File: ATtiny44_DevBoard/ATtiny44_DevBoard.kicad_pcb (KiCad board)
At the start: 2 copper layers, 48.3 x 42.5 mm, 19 parts, among them J1 Conn_01x08, J2 Conn_02x03_Odd_Even, J3 Conn_01x08, U1 ATtiny44A-SSU, Y1 Crystal 12MHz

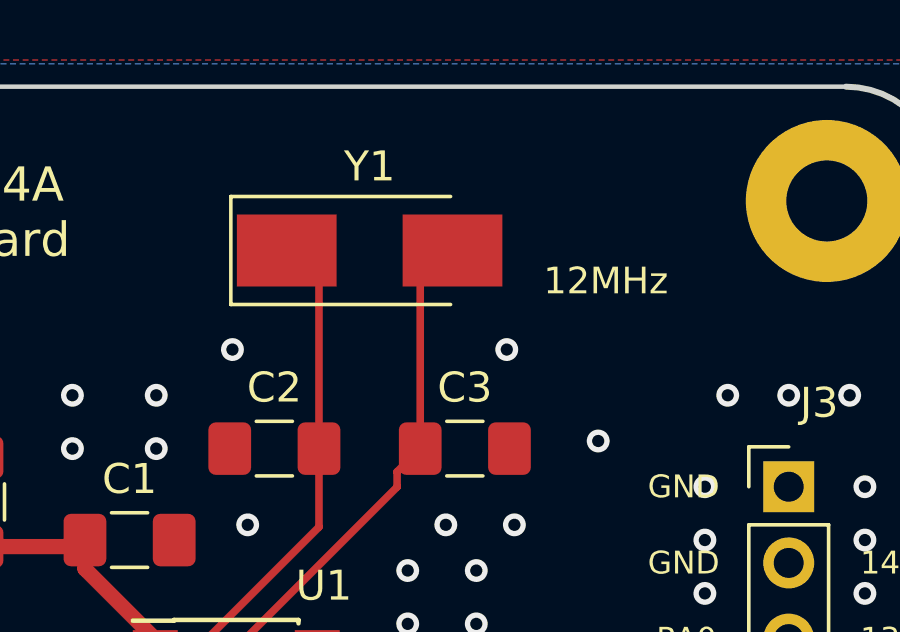
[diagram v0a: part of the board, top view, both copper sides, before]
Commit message: Replace SMD quartz with simpler THT one
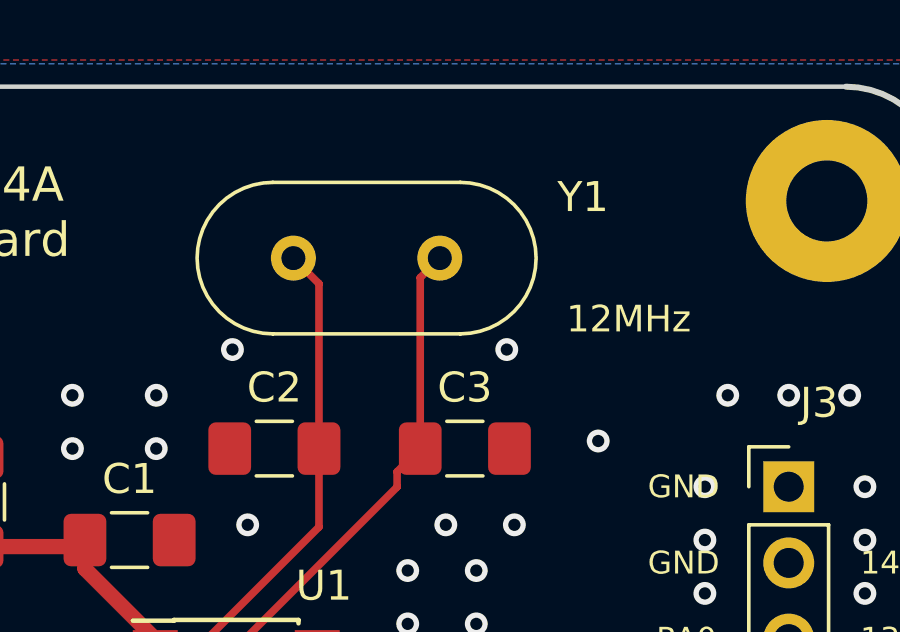
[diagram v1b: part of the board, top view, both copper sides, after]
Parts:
- Y1: footprint Crystal:Crystal_SMD_Abracon_ABM3-2Pin_5.0x3.2mm_HandSoldering -> Crystal:Crystal_HC49-U_Vertical
- moved Y1 2.55 mm to (150.9, 75.7)
- moved REF** 0.51 mm to (156.5, 80.3)
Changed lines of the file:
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@@
       (drillshape 0)
       (scaleselection 1)
-      (outputdirectory "gerber/"))
+      (outputdirectory "gerbers/"))
   )
   (net 0 "")
@@
     )
   )
-  (module Crystal:Crystal_SMD_Abracon_ABM3-2Pin_5.0x3.2mm_HandSoldering (layer F.Cu)
-    (at 153.416 75.438)
-    (descr "Abracon Miniature Ceramic Smd Crystal ABM3 http://www.abracon.com/Resonators/abm3.pdf, hand-soldering, 5.0x3.2mm^2 package")
-    (tags "SMD SMT crystal hand-soldering")
-    (attr smd)
-    (fp_text reference Y1 (at 0 -2.8) (layer F.SilkS)
-      (effects (font (size 1 1) (thickness 0.15)))
-    )
-    (fp_text value "Crystal 12MHz" (at 0 2.8) (layer F.Fab)
-      (effects (font (size 1 1) (thickness 0.15)))
-    )
-    (fp_text user %R (at 0 0) (layer F.Fab)
-      (effects (font (size 1 1) (thickness 0.15)))
-    )
-    (fp_line (start -2.3 -1.6) (end 2.3 -1.6) (layer F.Fab) (width 0.1))
-    (fp_line (start 2.3 -1.6) (end 2.5 -1.4) (layer F.Fab) (width 0.1))
-    (fp_line (start 2.5 -1.4) (end 2.5 1.4) (layer F.Fab) (width 0.1))
-    (fp_line (start 2.5 1.4) (end 2.3 1.6) (layer F.Fab) (width 0.1))
-    (fp_line (start 2.3 1.6) (end -2.3 1.6) (layer F.Fab) (width 0.1))
-    (fp_line (start -2.3 1.6) (end -2.5 1.4) (layer F.Fab) (width 0.1))
-    (fp_line (start -2.5 1.4) (end -2.5 -1.4) (layer F.Fab) (width 0.1))
-    (fp_line (start -2.5 -1.4) (end -2.3 -1.6) (layer F.Fab) (width 0.1))
-    (fp_line (start -2.5 0.6) (end -1.5 1.6) (layer F.Fab) (width 0.1))
-    (fp_line (start 2.7 -1.8) (end -4.625 -1.8) (layer F.SilkS) (width 0.12))
-    (fp_line (start -4.625 -1.8) (end -4.625 1.8) (layer F.SilkS) (width 0.12))
-    (fp_line (start -4.625 1.8) (end 2.7 1.8) (layer F.SilkS) (width 0.12))
-    (fp_line (start -4.7 -1.9) (end -4.7 1.9) (layer F.CrtYd) (width 0.05))
-    (fp_line (start -4.7 1.9) (end 4.7 1.9) (layer F.CrtYd) (width 0.05))
-    (fp_line (start 4.7 1.9) (end 4.7 -1.9) (layer F.CrtYd) (width 0.05))
-    (fp_line (start 4.7 -1.9) (end -4.7 -1.9) (layer F.CrtYd) (width 0.05))
-    (fp_circle (center 0 0) (end 0.5 0) (layer F.Adhes) (width 0.1))
-    (fp_circle (center 0 0) (end 0.416667 0) (layer F.Adhes) (width 0.166667))
-    (fp_circle (center 0 0) (end 0.266667 0) (layer F.Adhes) (width 0.166667))
-    (fp_circle (center 0 0) (end 0.116667 0) (layer F.Adhes) (width 0.233333))
-    (pad 1 smd rect (at -2.7625 0) (size 3.325 2.4) (layers F.Cu F.Paste F.Mask)
-      (net 3 /XTAL1))
-    (pad 2 smd rect (at 2.7625 0) (size 3.325 2.4) (layers F.Cu F.Paste F.Mask)
-      (net 4 /XTAL2))
-    (model ${KISYS3DMOD}/Crystal.3dshapes/Crystal_SMD_Abracon_ABM3-2Pin_5.0x3.2mm_HandSoldering.wrl
-      (at (xyz 0 0 0))
-      (scale (xyz 1 1 1))
-      (rotate (xyz 0 0 0))
-    )
-  )
   (module MountingHole:MountingHole_2.7mm_M2.5_Pad (layer F.Cu)
     (at 128.016 73.787)
@@
   )
   (module Symbol:KiCad-Logo2_6mm_SilkScreen (layer B.Cu)
-    (at 156.464 79.756 180)
+    (at 156.464 80.264 180)
     (descr "KiCad Logo")
     (tags "Logo KiCad")
@@
       (xy -2.549664 -1.91989) (xy -2.469928 -1.911165) (xy -2.400256 -1.919918)) (layer B.SilkS) (width 0.01))
   )
+  (module Crystal:Crystal_HC49-U_Vertical (layer F.Cu)
+    (at 150.876 75.692)
+    (descr "Crystal THT HC-49/U http://5hertz.com/pdfs/04404_D.pdf")
+    (tags "THT crystalHC-49/U")
+    (fp_text reference Y1 (at 9.652 -2.032) (layer F.SilkS)
+      (effects (font (size 1 1) (thickness 0.15)))
+    )
+    (fp_text value "Crystal 12MHz" (at 2.44 3.525) (layer F.Fab)
+      (effects (font (size 1 1) (thickness 0.15)))
+    )
+    (fp_text user %R (at 2.44 0) (layer F.Fab)
+      (effects (font (size 1 1) (thickness 0.15)))
+    )
+    (fp_line (start -0.685 -2.325) (end 5.565 -2.325) (layer F.Fab) (width 0.1))
+    (fp_line (start -0.685 2.325) (end 5.565 2.325) (layer F.Fab) (width 0.1))
+    (fp_line (start -0.56 -2) (end 5.44 -2) (layer F.Fab) (width 0.1))
+    (fp_line (start -0.56 2) (end 5.44 2) (layer F.Fab) (width 0.1))
+    (fp_line (start -0.685 -2.525) (end 5.565 -2.525) (layer F.SilkS) (width 0.12))
+    (fp_line (start -0.685 2.525) (end 5.565 2.525) (layer F.SilkS) (width 0.12))
+    (fp_line (start -3.5 -2.8) (end -3.5 2.8) (layer F.CrtYd) (width 0.05))
+    (fp_line (start -3.5 2.8) (end 8.4 2.8) (layer F.CrtYd) (width 0.05))
+    (fp_line (start 8.4 2.8) (end 8.4 -2.8) (layer F.CrtYd) (width 0.05))
+    (fp_line (start 8.4 -2.8) (end -3.5 -2.8) (layer F.CrtYd) (width 0.05))
+    (fp_arc (start -0.685 0) (end -0.685 -2.325) (angle -180) (layer F.Fab) (width 0.1))
+    (fp_arc (start 5.565 0) (end 5.565 -2.325) (angle 180) (layer F.Fab) (width 0.1))
+    (fp_arc (start -0.56 0) (end -0.56 -2) (angle -180) (layer F.Fab) (width 0.1))
+    (fp_arc (start 5.44 0) (end 5.44 -2) (angle 180) (layer F.Fab) (width 0.1))
+    (fp_arc (start -0.685 0) (end -0.685 -2.525) (angle -180) (layer F.SilkS) (width 0.12))
+    (fp_arc (start 5.565 0) (end 5.565 -2.525) (angle 180) (layer F.SilkS) (width 0.12))
+    (pad 1 thru_hole circle (at 0 0) (size 1.5 1.5) (drill 0.8) (layers *.Cu *.Mask)
+      (net 3 /XTAL1))
+    (pad 2 thru_hole circle (at 4.88 0) (size 1.5 1.5) (drill 0.8) (layers *.Cu *.Mask)
+      (net 4 /XTAL2))
+    (model ${KISYS3DMOD}/Crystal.3dshapes/Crystal_HC49-U_Vertical.wrl
+      (at (xyz 0 0 0))
+      (scale (xyz 1 1 1))
+      (rotate (xyz 0 0 0))
+    )
+  )
   (gr_text "Rev 1.0" (at 135.128 109.728) (layer F.SilkS)
     (effects (font (size 1.143 1.143) (thickness 0.1778)))
@@
     (effects (font (size 0.762 0.762) (thickness 0.127)))
   )
-  (gr_text 12MHz (at 161.29 76.454) (layer F.SilkS)
+  (gr_text 12MHz (at 162.052 77.724) (layer F.SilkS)
     (effects (font (size 0.889 0.889) (thickness 0.1524)))
   )
@@
   (segment (start 130.556 89.662) (end 129.286 88.392) (width 0.254) (layer F.Cu) (net 3) (status 20))
   (segment (start 146.271 89.662) (end 130.556 89.662) (width 0.254) (layer F.Cu) (net 3) (status 10))
-  (segment (start 151.7285 76.513) (end 150.6535 75.438) (width 0.254) (layer F.Cu) (net 3))
-  (segment (start 151.7285 82.042) (end 151.7285 76.513) (width 0.254) (layer F.Cu) (net 3))
+  (segment (start 151.7285 76.5445) (end 150.876 75.692) (width 0.254) (layer F.Cu) (net 3))
+  (segment (start 151.7285 82.042) (end 151.7285 76.5445) (width 0.254) (layer F.Cu) (net 3))
   (segment (start 146.721 90.932) (end 146.271 90.932) (width 0.254) (layer F.Cu) (net 4) (status 30))
   (segment (start 154.332153 83.320847) (end 146.721 90.932) (width 0.254) (layer F.Cu) (net 4) (status 20))
@@
   (segment (start 155.1035 82.042) (end 154.332153 82.813347) (width 0.254) (layer F.Cu) (net 4) (status 10))
   (segment (start 146.271 90.932) (end 129.286 90.932) (width 0.254) (layer F.Cu) (net 4) (status 30))
-  (segment (start 155.1035 76.513) (end 156.1785 75.438) (width 0.254) (layer F.Cu) (net 4))
-  (segment (start 155.1035 82.042) (end 155.1035 76.513) (width 0.254) (layer F.Cu) (net 4))
+  (segment (start 155.1035 76.3445) (end 155.756 75.692) (width 0.254) (layer F.Cu) (net 4))
+  (segment (start 155.1035 82.042) (end 155.1035 76.3445) (width 0.254) (layer F.Cu) (net 4))
   (segment (start 159.004 107.6595) (end 158.496 107.1515) (width 0.254) (layer F.Cu) (net 5) (status 30))
   (segment (start 163.322 107.6595) (end 159.004 107.6595) (width 0.254) (layer F.Cu) (net 5) (status 30))

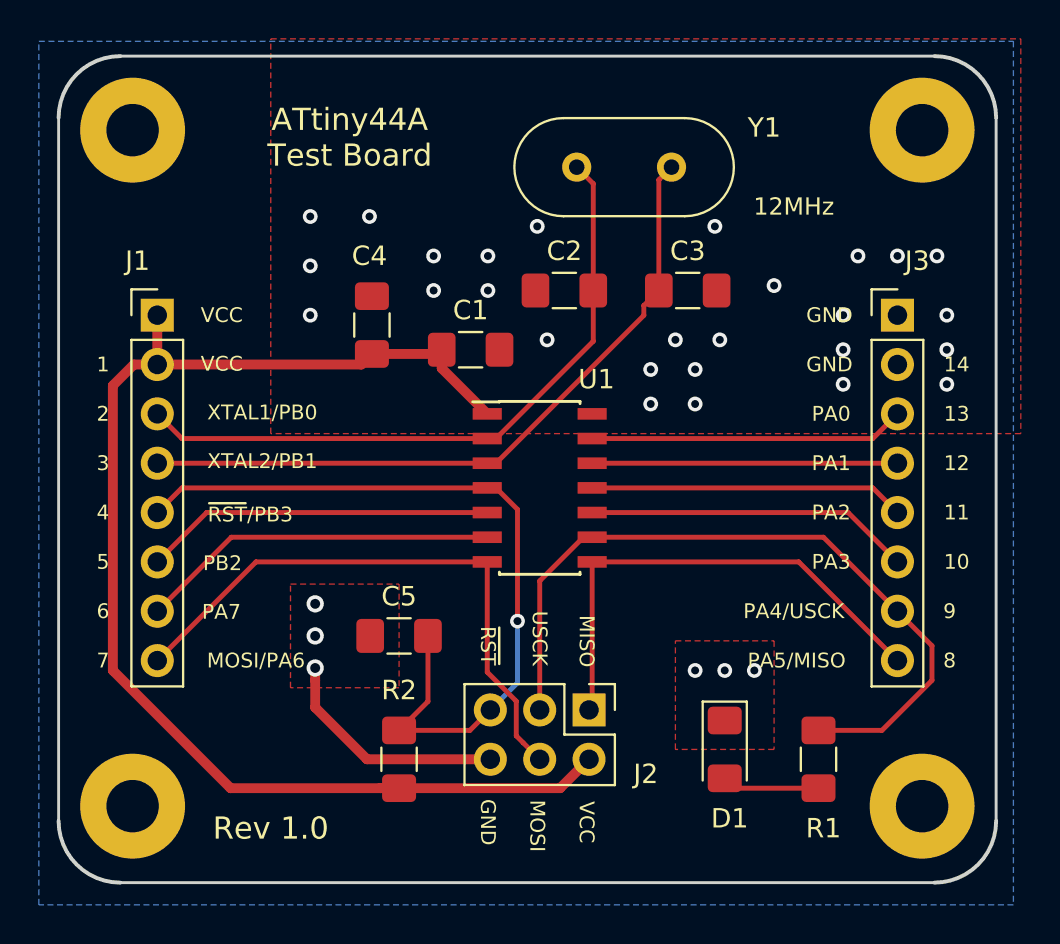
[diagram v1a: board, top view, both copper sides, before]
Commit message: Update ATtiny44_DevBoard.kicad_pcb
Connect mounting hole pads to GND
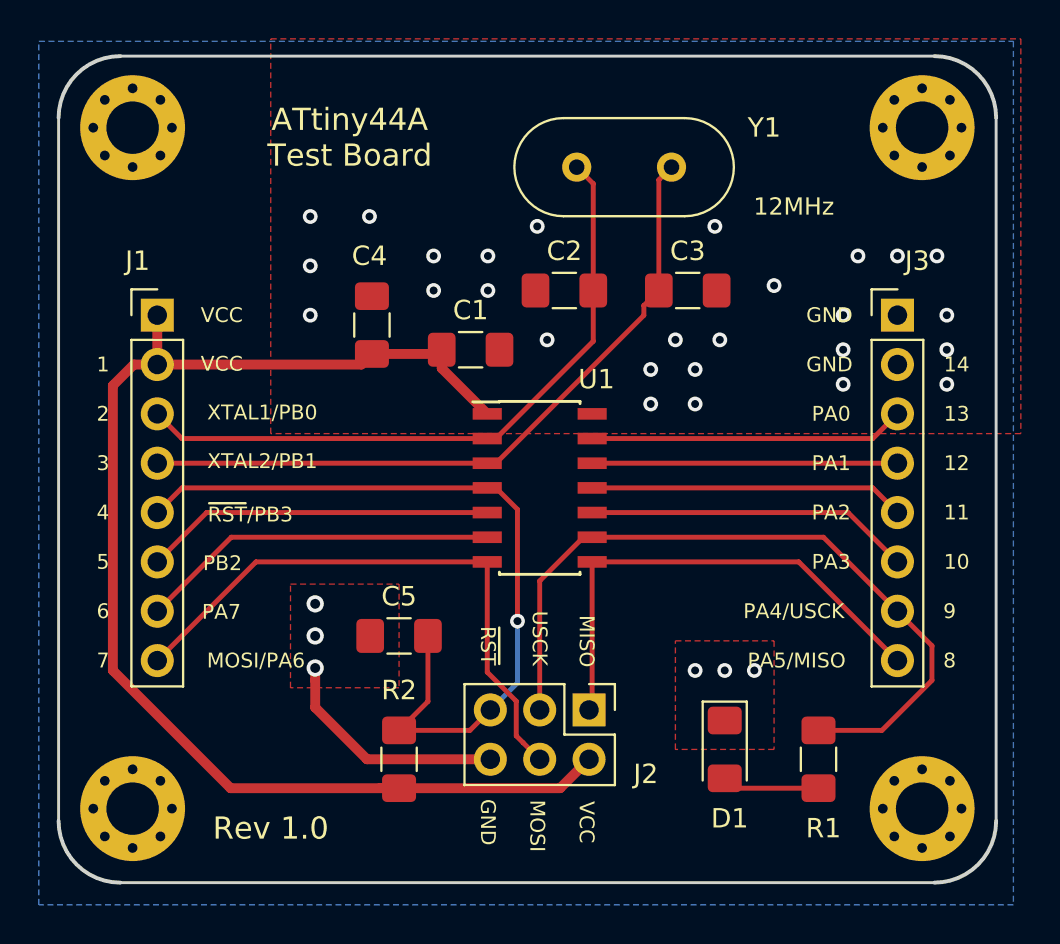
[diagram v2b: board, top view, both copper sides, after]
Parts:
- removed the REF** at (128.0, 73.8)
- removed the REF** at (168.7, 73.8)
- removed the REF** at (168.7, 108.6)
- removed the REF** at (128.0, 108.6)
- added REF**: MountingHole_2.7mm_M2.5_Pad_Via, MountingHole:MountingHole_2.7mm_M2.5_Pad_Via, F.Cu at (128.0, 108.7)
- added REF**: MountingHole_2.7mm_M2.5_Pad_Via, MountingHole:MountingHole_2.7mm_M2.5_Pad_Via, F.Cu at (128.0, 73.7)
- added REF**: MountingHole_2.7mm_M2.5_Pad_Via, MountingHole:MountingHole_2.7mm_M2.5_Pad_Via, F.Cu at (168.7, 73.7)
- added REF**: MountingHole_2.7mm_M2.5_Pad_Via, MountingHole:MountingHole_2.7mm_M2.5_Pad_Via, F.Cu at (168.7, 108.7)

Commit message: Improvements after critique from Reddit
- Made the traces larger: now signal is 16mils and Power is 30mils
- Removed redundant trace to GND on the ISP header
- Routed MOSI differently to avoid unnecessary trace on the bottom plane
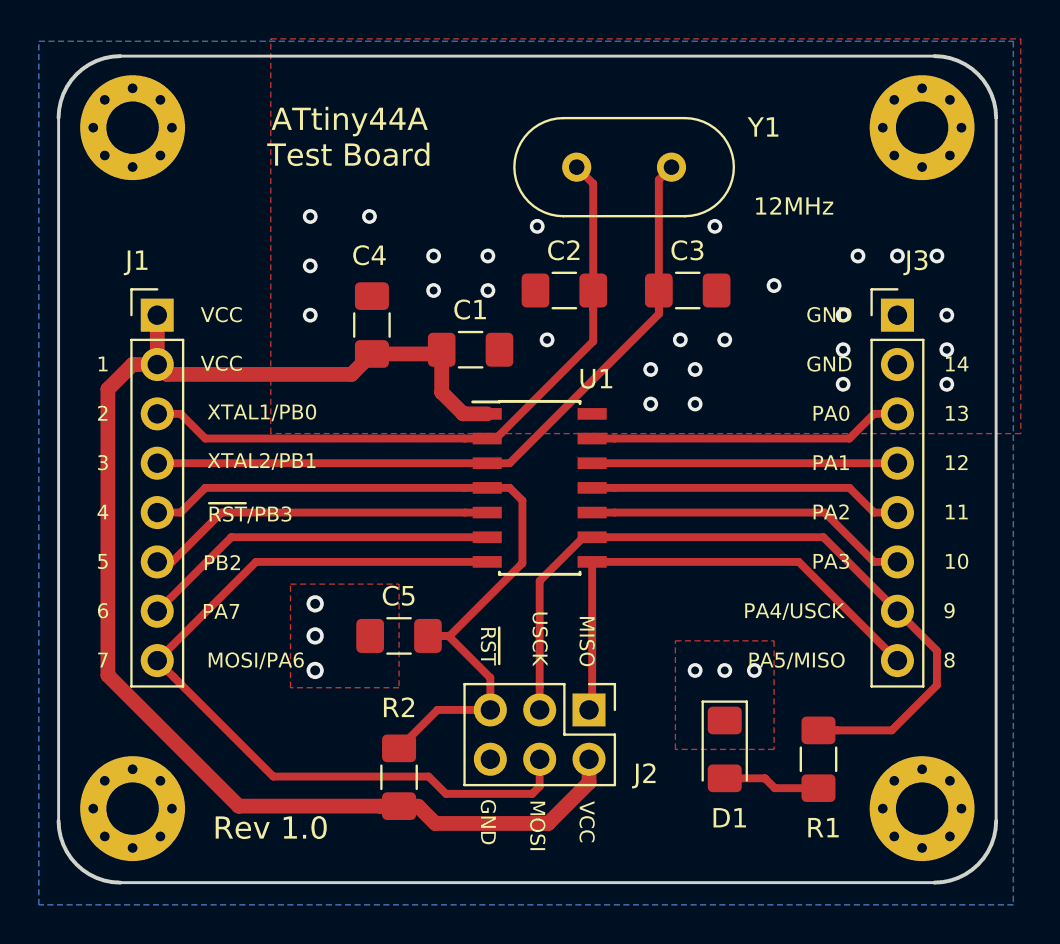
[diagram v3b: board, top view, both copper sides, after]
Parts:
- moved R2 0.93 mm to (141.7, 107.1)
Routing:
- net /MOSI: track 30.4 -> 43.2 mm
- net GND: track 12.2 -> 0.00 mm
- net VCC: track 66.8 -> 70.7 mm
- net /~RESET: track 41.0 -> 40.5 mm, vias 1 -> 0
- net /USCK: track 38.8 -> 39.3 mm
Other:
- net class Default: clearance 0.2286 -> 0.254; trace_width 0.254 -> 0.4064
- net class Power: clearance 0.2286 -> 0.254; trace_width 0.508 -> 0.762
- rule trace_clearance: 0.2286 -> 0.254

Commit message: Move the crystal closer to the chip
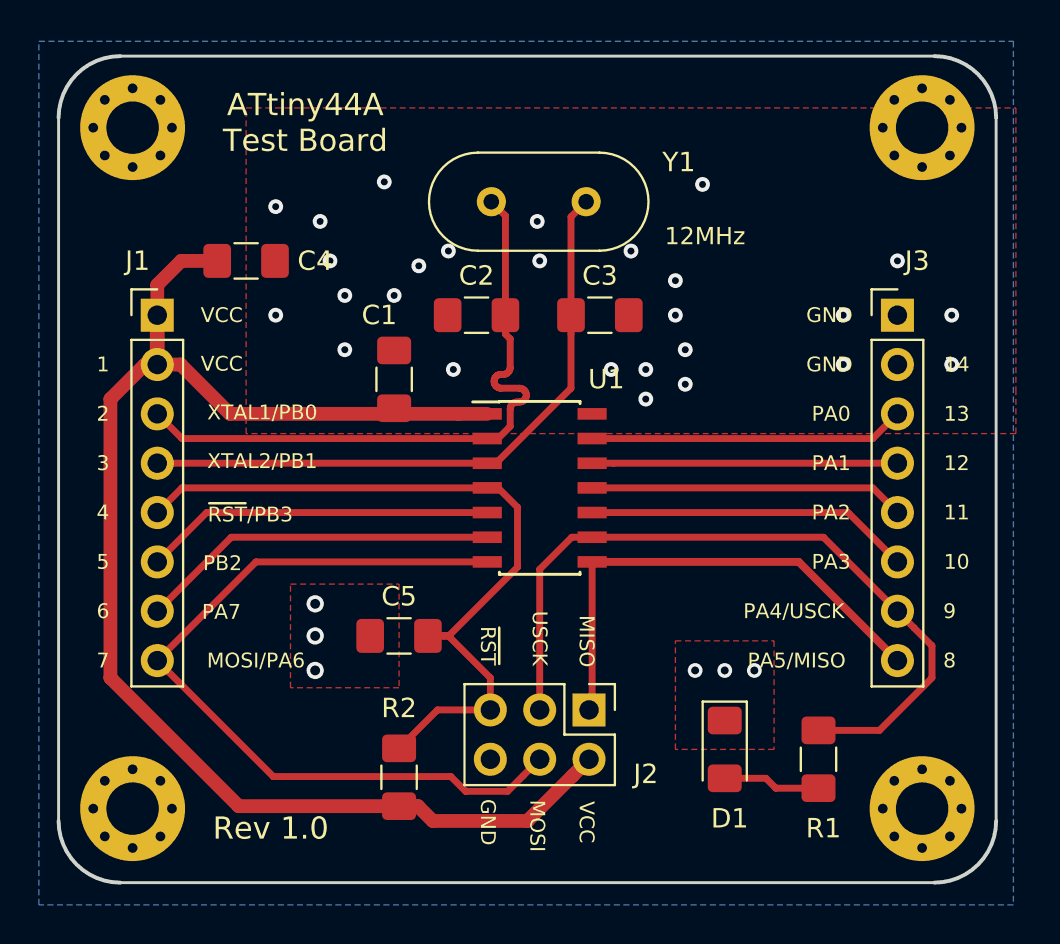
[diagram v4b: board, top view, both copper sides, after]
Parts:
- moved C4 7.27 mm to (133.9, 80.5), turned to 0 degrees
- moved Y1 4.74 mm to (146.5, 77.5)
- moved C2 4.70 mm to (145.7, 83.3)
- moved C3 4.70 mm to (152.1, 83.3)
- moved C1 4.22 mm to (141.5, 86.6), turned to 90 degrees
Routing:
- net /XTAL2: track 36.8 -> 32.8 mm
- net VCC: track 70.7 -> 72.2 mm
- net /XTAL1: track 34.4 -> 33.3 mm
- net /MOSI: track 43.2 -> 42.2 mm
- net /~RESET: track 40.5 -> 39.9 mm
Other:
- net class Default: trace_width 0.4064 -> 0.3556; via_drill 0.4064 -> 0.3556
- net class Power: trace_width 0.762 -> 0.7112

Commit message: Improve decoupling capacitors placement
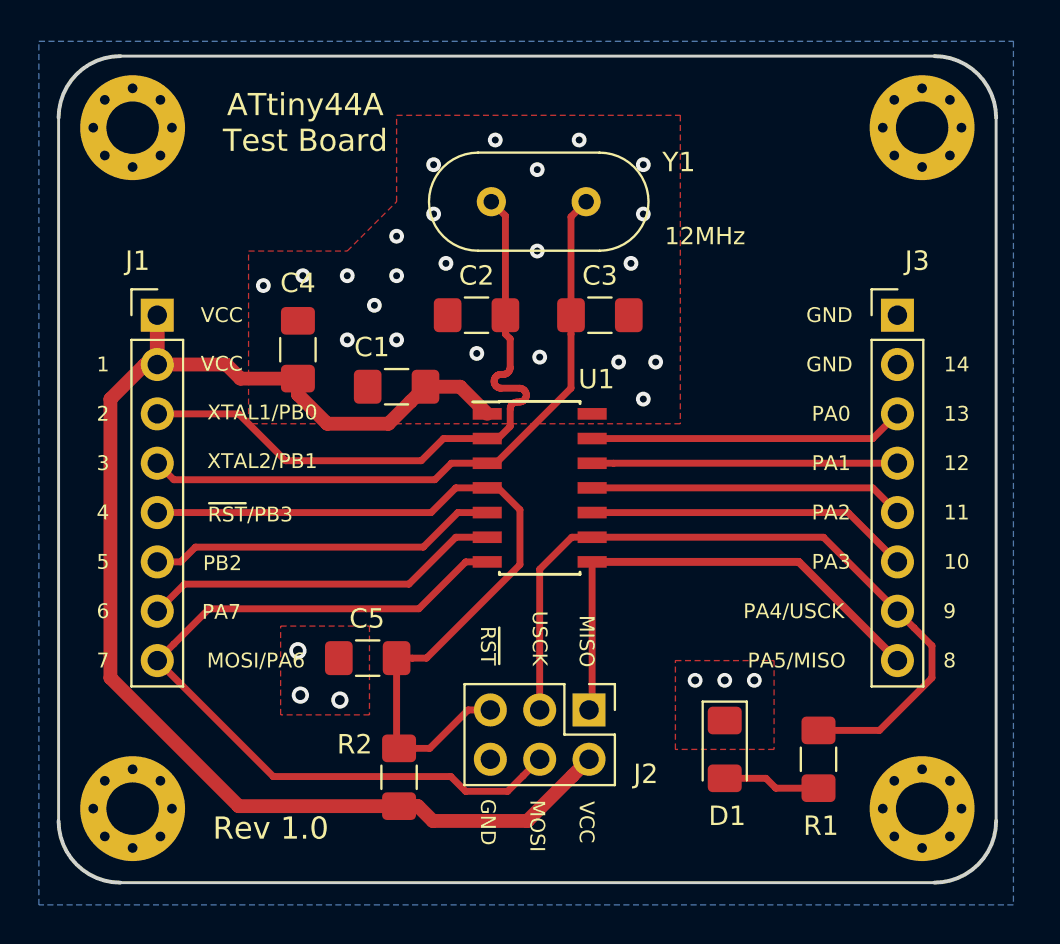
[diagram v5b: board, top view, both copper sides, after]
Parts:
- moved C4 5.29 mm to (136.5, 85.1), turned to 90 degrees
- moved REF** 3.30 mm to (135.9, 98.0)
- moved C5 1.98 mm to (140.1, 101.0)
- moved REF** 1.93 mm to (157.2, 82.0)
- moved C1 0.40 mm to (141.6, 87.0), turned to 180 degrees
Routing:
- net VCC: track 72.2 -> 69.1 mm
- net /~RESET: track 39.9 -> 41.0 mm
- net /XTAL1: track 33.3 -> 34.3 mm
- net /XTAL2: track 32.8 -> 33.5 mm
- net GND: vias 33 -> 29
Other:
- board text added: "github.com/acisternino/dev-board-attiny44a"
